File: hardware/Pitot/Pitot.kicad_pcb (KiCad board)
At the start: 2 copper layers, 52.2 x 61.5 mm, 54 parts, among them IC1 ABPMRRV060MG2A3, IC2 ABPMRRV060MG2A3, J1 53307-2471, J3 MX150_02x06_Vertical, J4 Conn_01x07, U2 LDO40LPURY

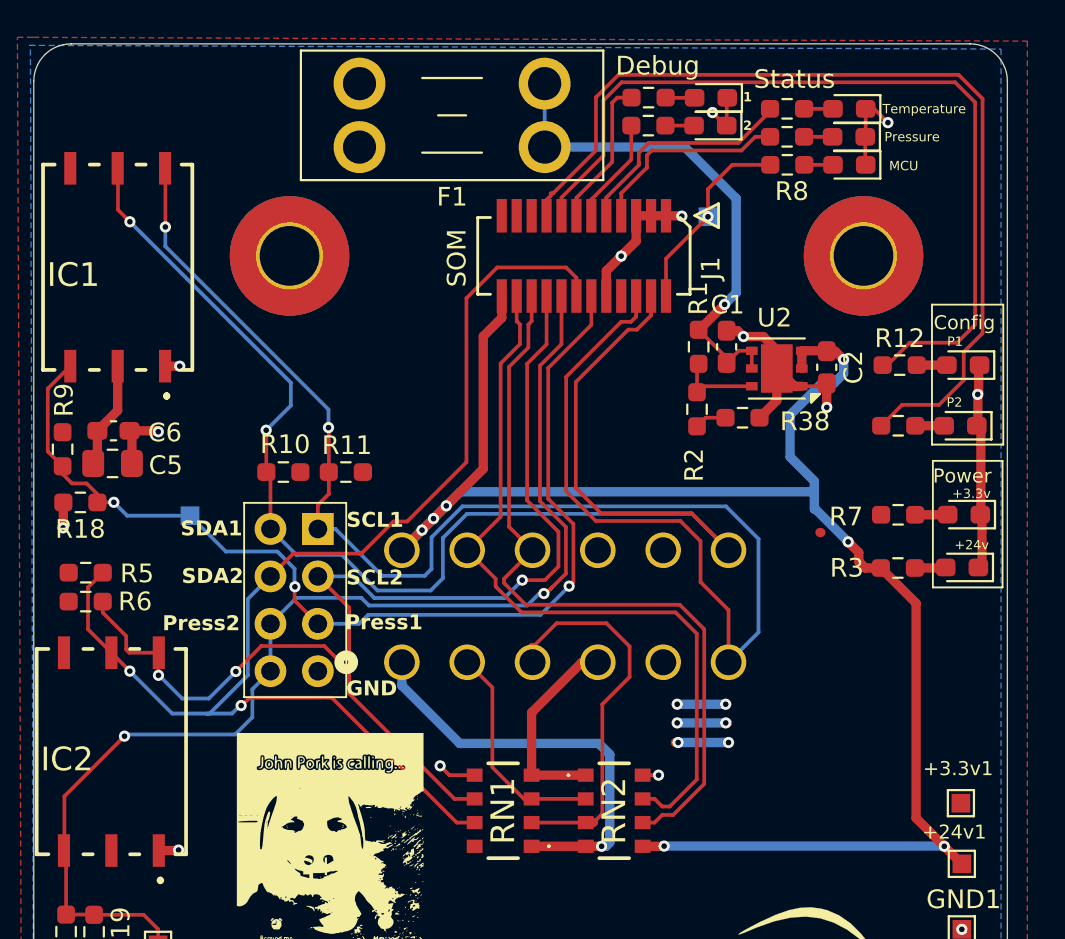
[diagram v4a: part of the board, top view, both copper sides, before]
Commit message: .bom files generated, cleaned up pitot board.
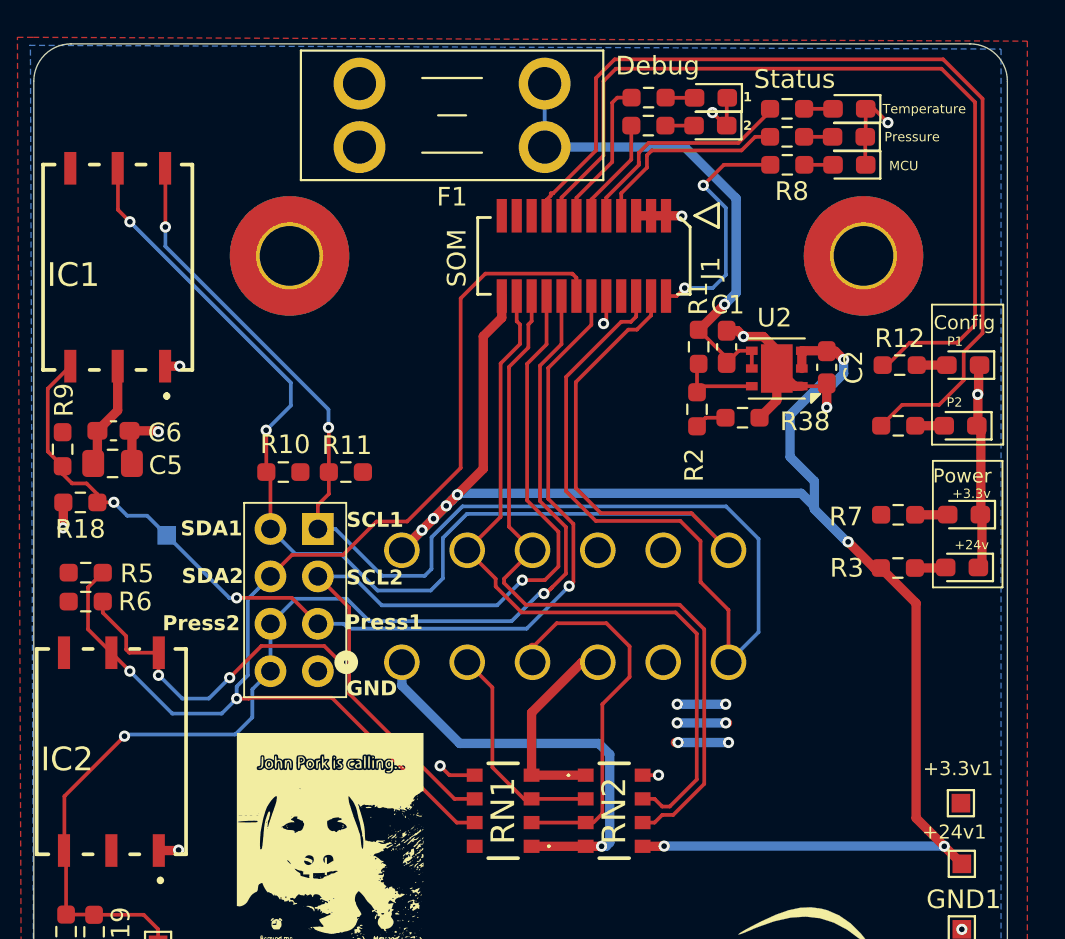
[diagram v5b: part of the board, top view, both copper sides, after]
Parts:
- removed +3.3MCU1: TestPoint, TestPoint:TestPoint_Pad_1.0x1.0mm
- moved PressERR1 1.63 mm to (64.2, 58.5)
- moved G*** 0.77 mm to (64.5, 35.2)
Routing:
- net GND: track 48.7 -> 45.2 mm
- net +3.3VMCU: track 10.6 -> 13.1 mm, vias 1 -> 2
- net /SDA2: track 67.5 -> 65.9 mm
- net /P2_LED: track 50.2 -> 51.5 mm
- net /P1_LED: track 45.6 -> 46.8 mm
- net +24V: track 91.8 -> 92.9 mm, vias 7 -> 8
- net /pressERR_1: track 56.3 -> 55.5 mm
- net /pressERR_2: track 63.4 -> 64.1 mm
